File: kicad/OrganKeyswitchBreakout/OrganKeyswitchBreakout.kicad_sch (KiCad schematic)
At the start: 22 parts, among them U1 MCP23017_SS, U2 MCP23017_SS

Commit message: Finalized v001 of MCU board for production
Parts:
- removed CD_U1, CD_U2: 100n, symbol Device:C
- removed JP1, JP2, JP3, JP4, JP5, JP6: A2 0/1, symbol Jumper:SolderJumper_2_Open
- removed R1, R10, R2, R3, R4, R7, R8, R9: 10k, symbol Device:R_US
- removed U1, U2: MCP23017_SS, Package_SO:SSOP-28_5.3x10.2mm_P0.65mm, symbol Interface_Expansion:MCP23017_SS
- added JP_INT_PU1: INT Pullup, symbol Jumper:SolderJumper_2_Open
- added R11: 4.7k, symbol Device:R_US
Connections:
- net +3.3V: now also R11.1
- net SCL: no longer names the net of JP_SCL_PU1.1 (A)
- net SDA: no longer names the net of JP_SDA_PU1.1 (A)
- new net: JP_INT_PU1.2 (B), R11.2
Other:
- added sheet breakout_chip (breakout_chip.kicad_sch)
- moved on the sheet: JP_SCL_PU1, JP_SDA_PU1, R5, R6

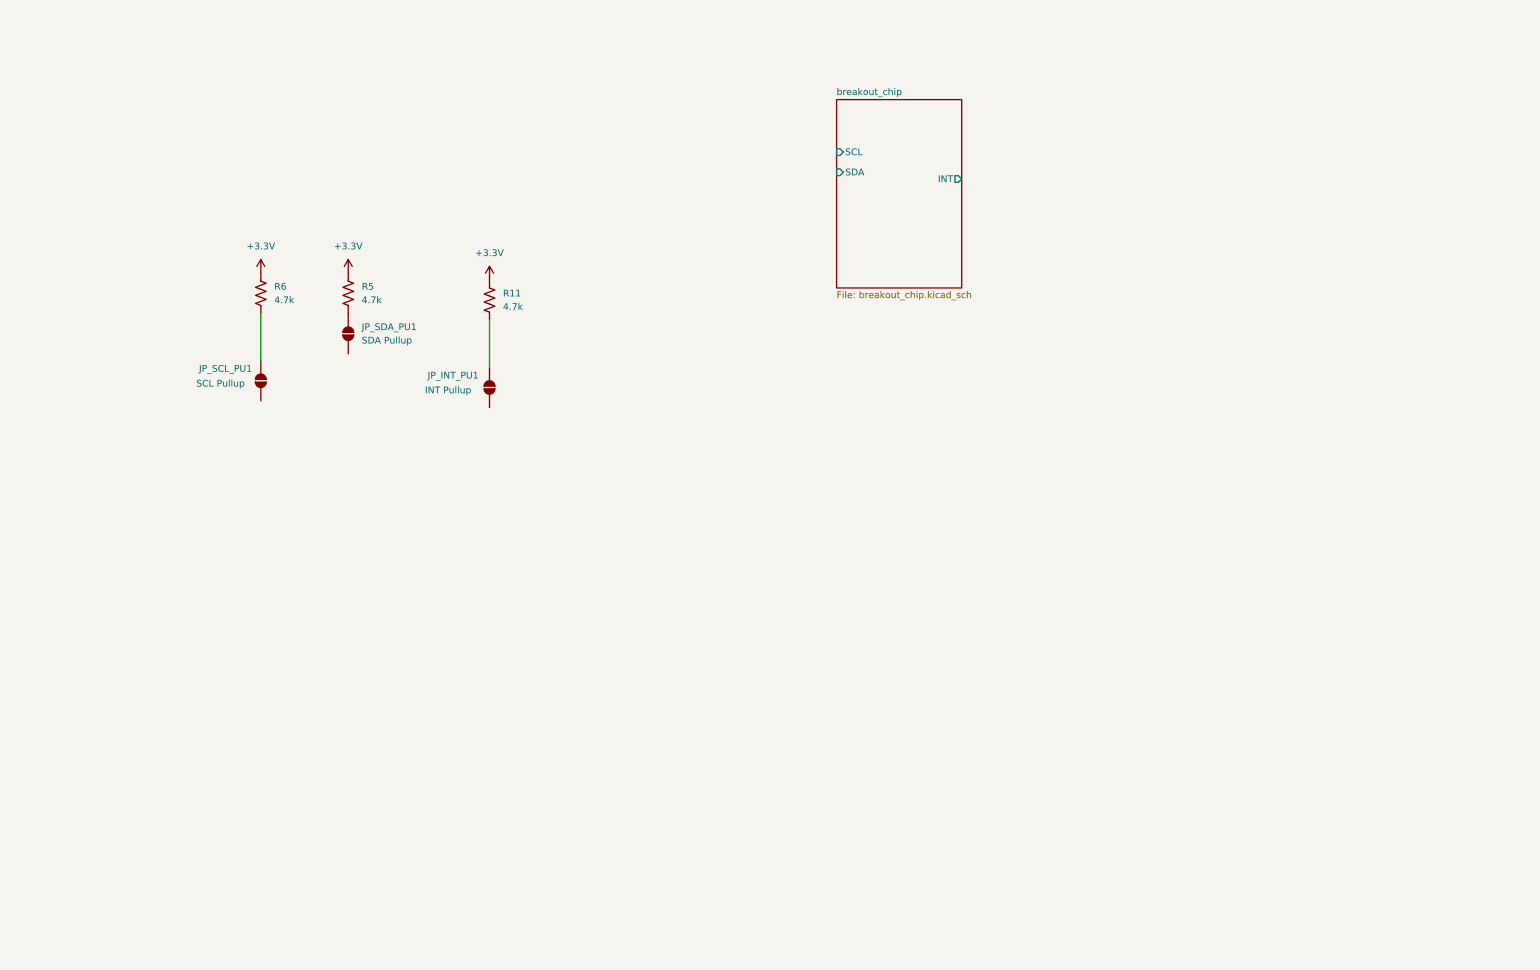
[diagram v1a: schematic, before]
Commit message: Finishing keyswitch breakout board
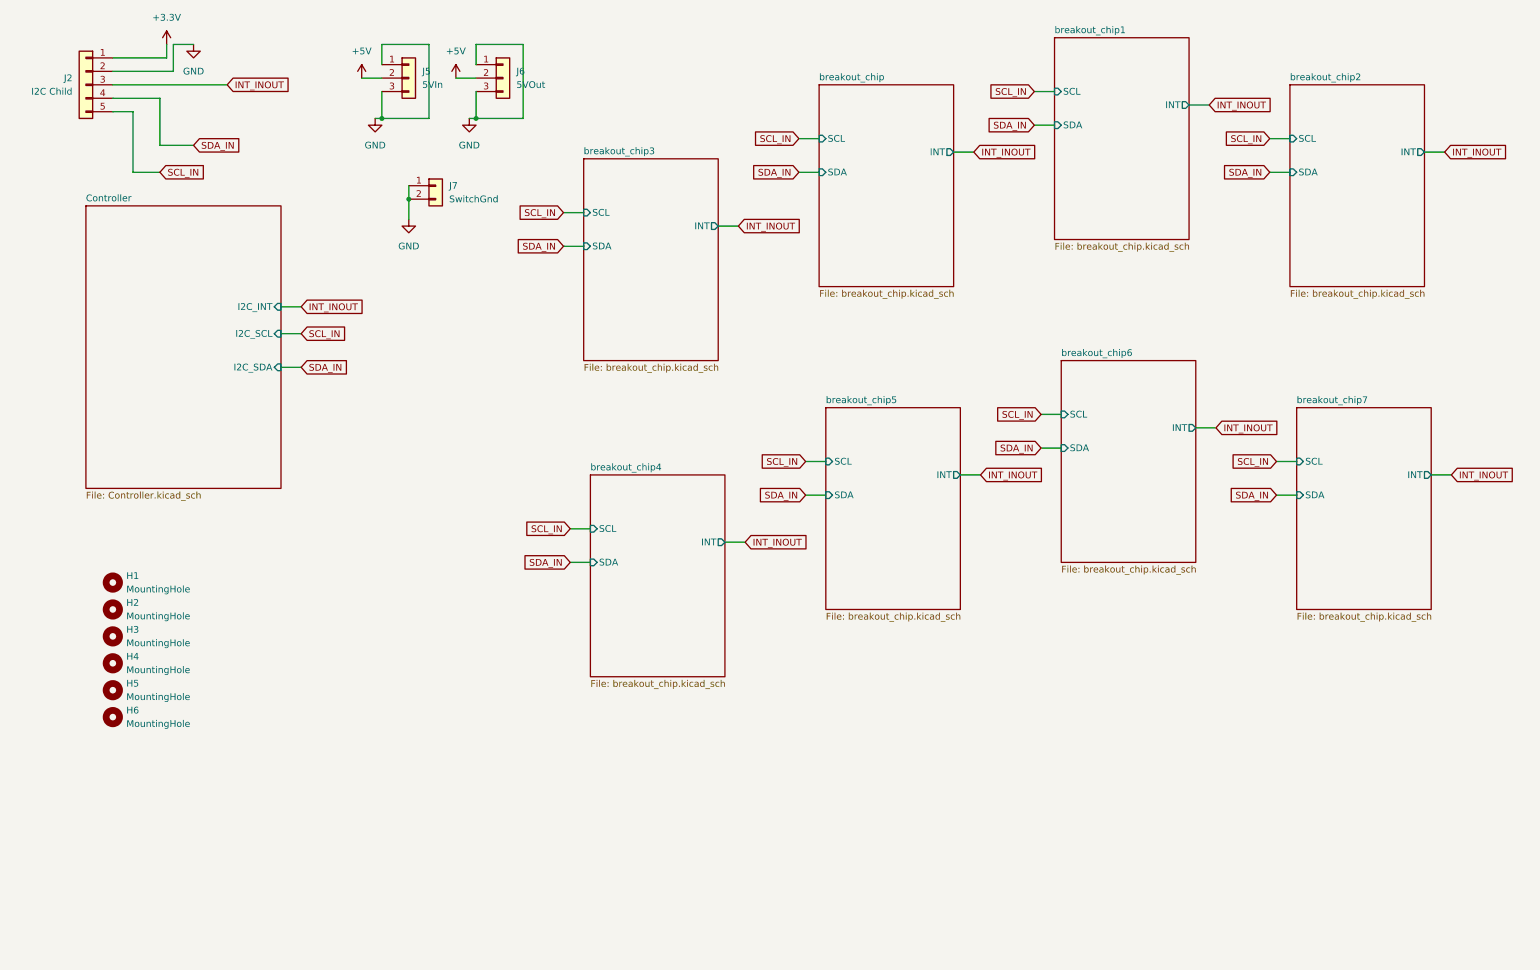
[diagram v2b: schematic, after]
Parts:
- removed JP_INT_PU1: INT Pullup, symbol Jumper:SolderJumper_2_Open
- removed JP_SCL_PU1: SCL Pullup, symbol Jumper:SolderJumper_2_Open
- removed JP_SDA_PU1: SDA Pullup, symbol Jumper:SolderJumper_2_Open
- removed R11, R5, R6: 4.7k, symbol Device:R_US
- added H1, H2, H3, H4, H5, H6: MountingHole, MountingHole:MountingHole_3.2mm_M3, symbol Mechanical:MountingHole
- added J2: I2C Child, Connector_JST:JST_PH_B5B-PH-K_1x05_P2.00mm_Vertical, symbol Connector_Generic:Conn_01x05
- added J5: 5VIn, Connector_JST:JST_PH_B3B-PH-K_1x03_P2.00mm_Vertical, symbol Connector_Generic:Conn_01x03
- added J6: 5VOut, Connector_JST:JST_PH_B3B-PH-K_1x03_P2.00mm_Vertical, symbol Connector_Generic:Conn_01x03
- added J7: SwitchGnd, Connector_JST:JST_PH_B2B-PH-K_1x02_P2.00mm_Vertical, symbol Connector_Generic:Conn_01x02
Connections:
- net +3.3V: now also J2.1 (Pin_1)
- new net +5V: J5.2 (Pin_2), J6.2 (Pin_2)
- new net GND: J2.2 (Pin_2), J5.1 (Pin_1), J5.3 (Pin_3), J6.1 (Pin_1), J6.3 (Pin_3), J7.1 (Pin_1), J7.2 (Pin_2)
- new net INT_INOUT: J2.3 (Pin_3)
- new net SCL_IN: J2.5 (Pin_5)
- new net SDA_IN: J2.4 (Pin_4)
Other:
- added sheet Controller (Controller.kicad_sch)
- added sheet breakout_chip1 (breakout_chip.kicad_sch)
- added sheet breakout_chip2 (breakout_chip.kicad_sch)
- added sheet breakout_chip3 (breakout_chip.kicad_sch)
- added sheet breakout_chip4 (breakout_chip.kicad_sch)
- added sheet breakout_chip5 (breakout_chip.kicad_sch)
- added sheet breakout_chip6 (breakout_chip.kicad_sch)
- added sheet breakout_chip7 (breakout_chip.kicad_sch)

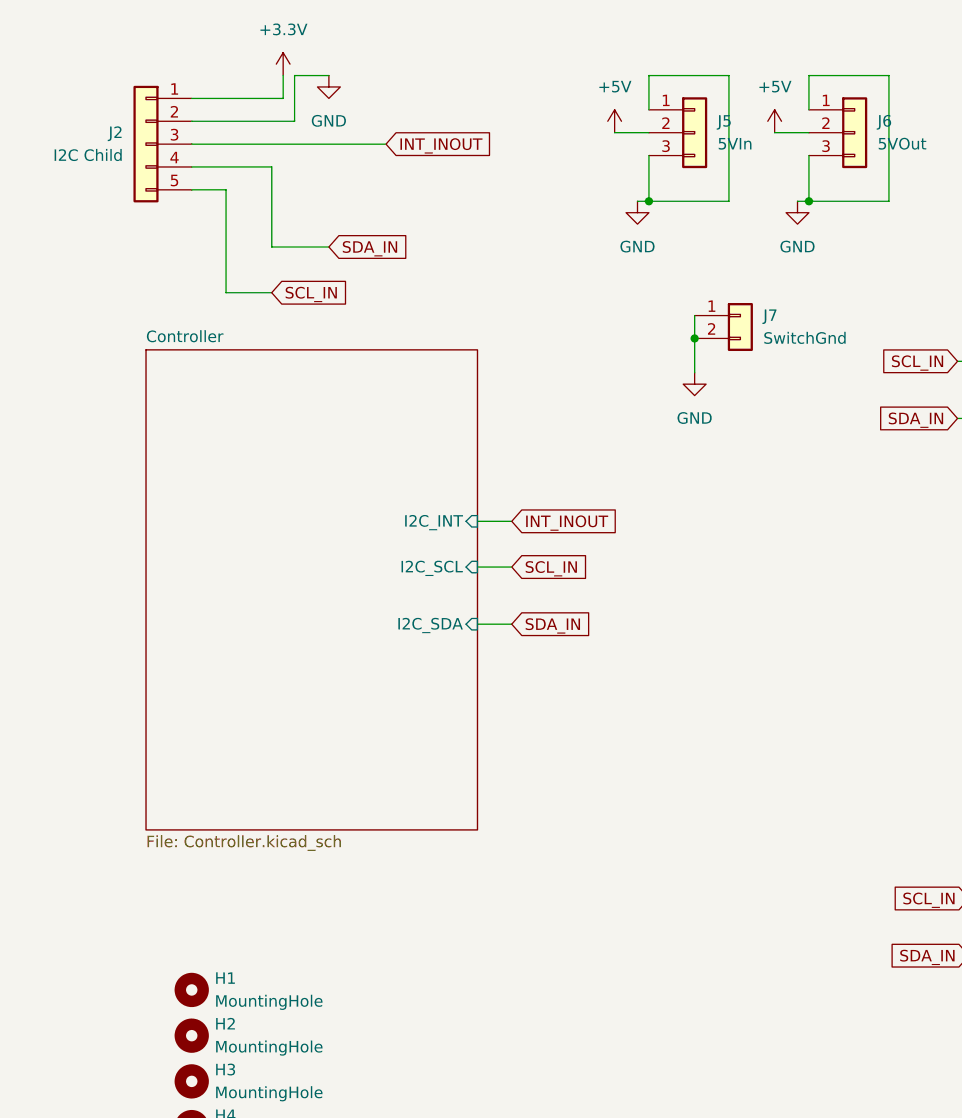
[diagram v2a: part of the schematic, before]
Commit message: Adding keyswitch breakout system, and some tools
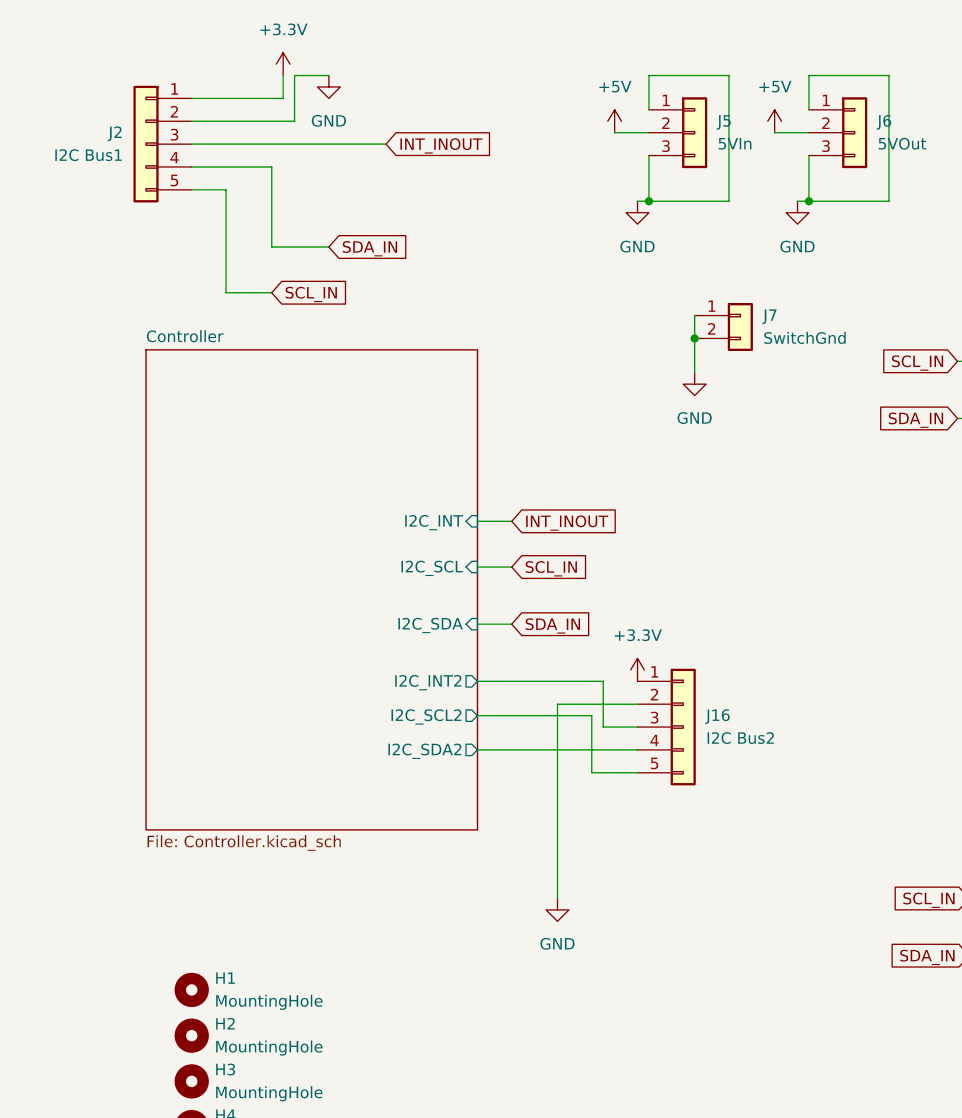
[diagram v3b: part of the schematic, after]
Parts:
- added J16: I2C Bus2, Connector_JST:JST_PH_B5B-PH-K_1x05_P2.00mm_Vertical, symbol Connector_Generic:Conn_01x05
- J2: value I2C Child -> I2C Bus1
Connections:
- net +3.3V: now also J16.1 (Pin_1)
- net GND: now also J16.2 (Pin_2)
- new net Controller/I2C_INT2: J16.3 (Pin_3)
- new net Controller/I2C_SCL2: J16.5 (Pin_5)
- new net Controller/I2C_SDA2: J16.4 (Pin_4)
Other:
- sheet Controller ports: added I2C_INT2, I2C_SCL2, I2C_SDA2; removed none
